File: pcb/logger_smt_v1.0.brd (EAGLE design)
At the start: 59.8 x 53.3 mm, 33 parts, among them J1 MICRO-SDCARD-CONNECTOR-330006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, U1 DS1307ZN-1900100P1, U2 CJ1117-3.3-1310190P1, U3 74VHCT125PW, X1 32.768KHZ

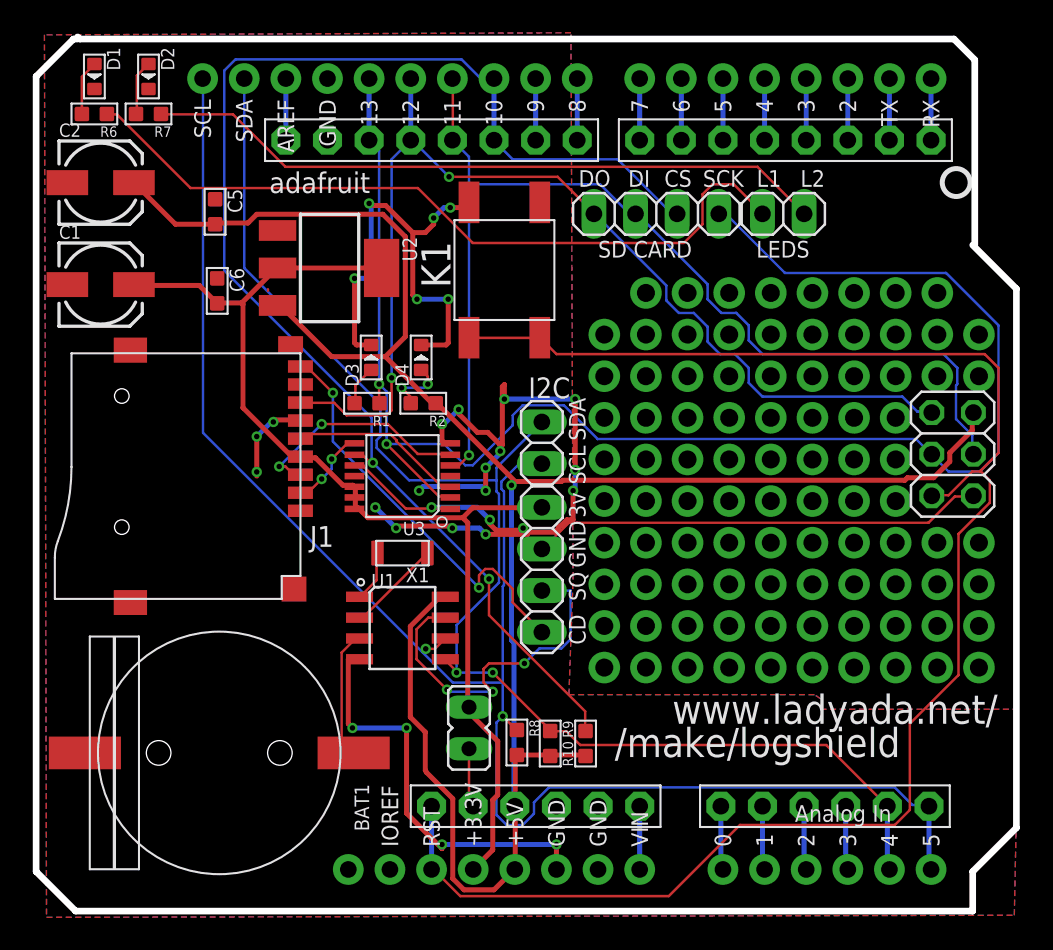
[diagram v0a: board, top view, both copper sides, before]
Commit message: Changed attribution and removed adafruit trademark
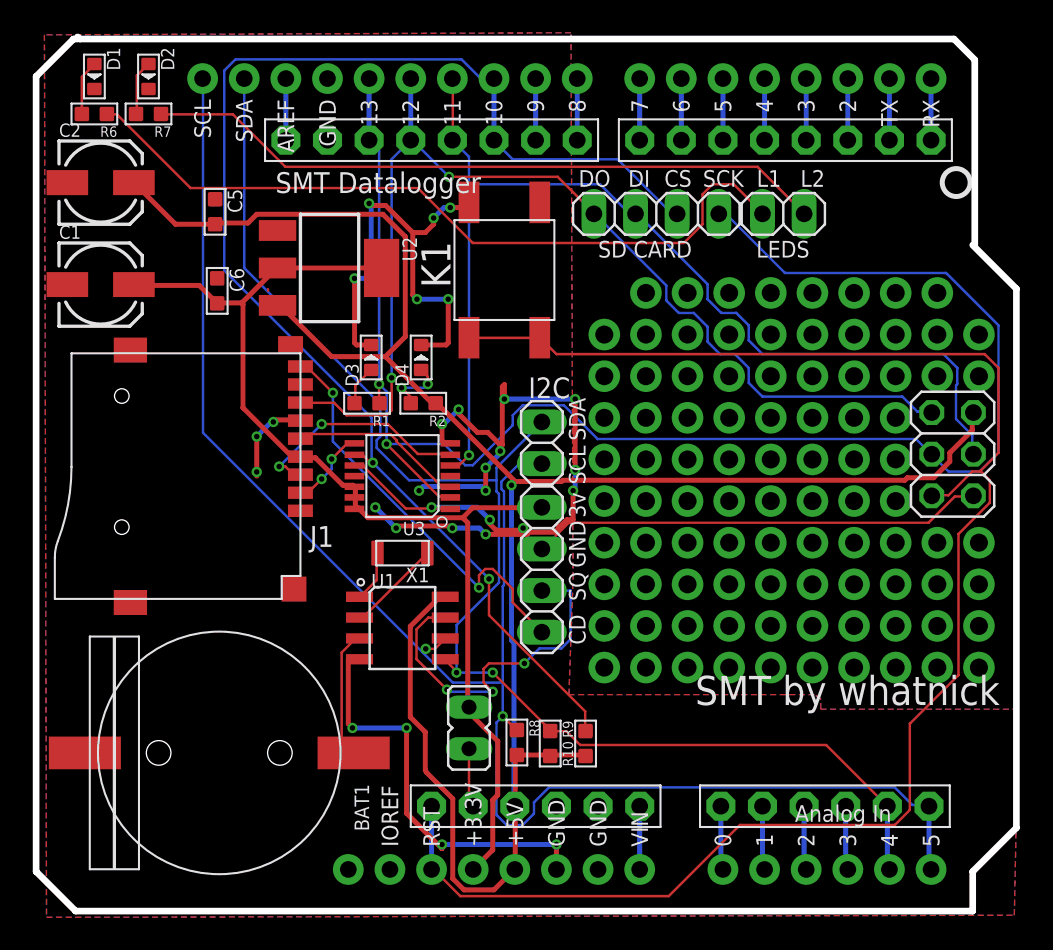
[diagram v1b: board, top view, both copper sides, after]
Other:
- board text added: "SMT Datalogger"
- board text added: "SMT by whatnick"
- board text removed: "/make/logshield"
- board text removed: "adafruit"
- board text removed: "make/logshield"
- board text removed: "www.ladyada.net/"
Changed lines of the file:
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@@
 <layer number="27" name="tValues" color="7" fill="1" visible="yes" active="yes"/>
 <layer number="28" name="bValues" color="7" fill="1" visible="yes" active="yes"/>
-<layer number="29" name="tStop" color="7" fill="3" visible="yes" active="yes"/>
-<layer number="30" name="bStop" color="7" fill="6" visible="yes" active="yes"/>
+<layer number="29" name="tStop" color="7" fill="3" visible="no" active="yes"/>
+<layer number="30" name="bStop" color="7" fill="6" visible="no" active="yes"/>
 <layer number="31" name="tCream" color="7" fill="4" visible="yes" active="yes"/>
 <layer number="32" name="bCream" color="7" fill="5" visible="yes" active="yes"/>
@@
 <text x="42.926" y="18.923" size="1.016" layer="21" font="vector" rot="R90">SQ</text>
 <text x="42.926" y="16.256" size="1.016" layer="21" font="vector" rot="R90">CD</text>
-<text x="68.072" y="13.208" size="1.778" layer="21" font="vector" rot="R180">www.ladyada.net/</text>
-<text x="44.704" y="9.398" size="1.778" layer="21" font="vector">/make/logshield</text>
-<text x="21.717" y="17.018" size="1.9304" layer="22" font="vector" rot="MR90">www.ladyada.net/</text>
-<text x="21.082" y="40.894" size="1.9304" layer="22" font="vector" rot="MR270">make/logshield</text>
-<text x="23.622" y="43.815" size="1.27" layer="21" font="vector">adafruit</text>
+<text x="68.199" y="14.351" size="1.778" layer="21" font="vector" rot="R180">SMT by whatnick</text>
+<text x="22.987" y="17.78" size="1.9304" layer="22" font="vector" rot="MR90">SMT by whatnick</text>
+<text x="24.003" y="43.815" size="1.27" layer="21" font="vector">SMT Datalogger</text>
 <wire x1="11.938" y1="53.213" x2="11.684" y2="53.213" width="0.4064" layer="20"/>
 <wire x1="11.684" y1="53.213" x2="9.398" y2="50.927" width="0.4064" layer="20"/>
